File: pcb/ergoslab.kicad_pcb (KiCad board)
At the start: 2 copper layers, 114.5 x 101.4 mm, 102 parts, among them J1 L_B_LED, J2 R_B_LED, J3 SLAVE_LED, P1 OLED, P2 ICSP, SW0:0 SW_Push, SW0:1 SW_Push, SW0:2 SW_Push, SW0:3 SW_Push, SW0:4 SW_Push, SW1:0 SW_Push, SW1:1 SW_Push, SW1:2 SW_Push, SW1:3 SW_Push, SW1:4 SW_Push, SW2:0 SW_Push, SW2:1 SW_Push, SW2:2 SW_Push, SW2:3 SW_Push, SW2:4 SW_Push, SW3:0 SW_Push, SW3:1 SW_Push, SW3:2 SW_Push, SW3:3 SW_Push, SW3:4 SW_Push, SW3:5 SW_Push, SW4:1 SW_Push, SW4:2 SW_Push, SW4:3 SW_Push, SW4:4 SW_Push, SW4:5 SW_Push

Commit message: feat: update chicken
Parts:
- removed the REF** at (163.8, 88.2)
- added G***: LOGO, footprints:chicken, B.Cu at (177.5, 71.1)
- moved REF** 2.54 mm to (137.6, 46.5)
- moved REF** 1.78 mm to (163.6, 49.8)
- moved REF** 1.25 mm to (125.6, 120.5)
- moved REF** 1.14 mm to (106.2, 45.9)
- moved Drill 0.69 mm to (142.2, 123.5)
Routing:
- net Row3: track 153.2 -> 152.6 mm
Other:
- board size 114.5 x 101.4 mm -> 114.5 x 101.2 mm

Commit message: docs: add list of parts to order
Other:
- outline, holes or cut-outs redrawn
- board text added: "FIXME still need hole when we put LED here"

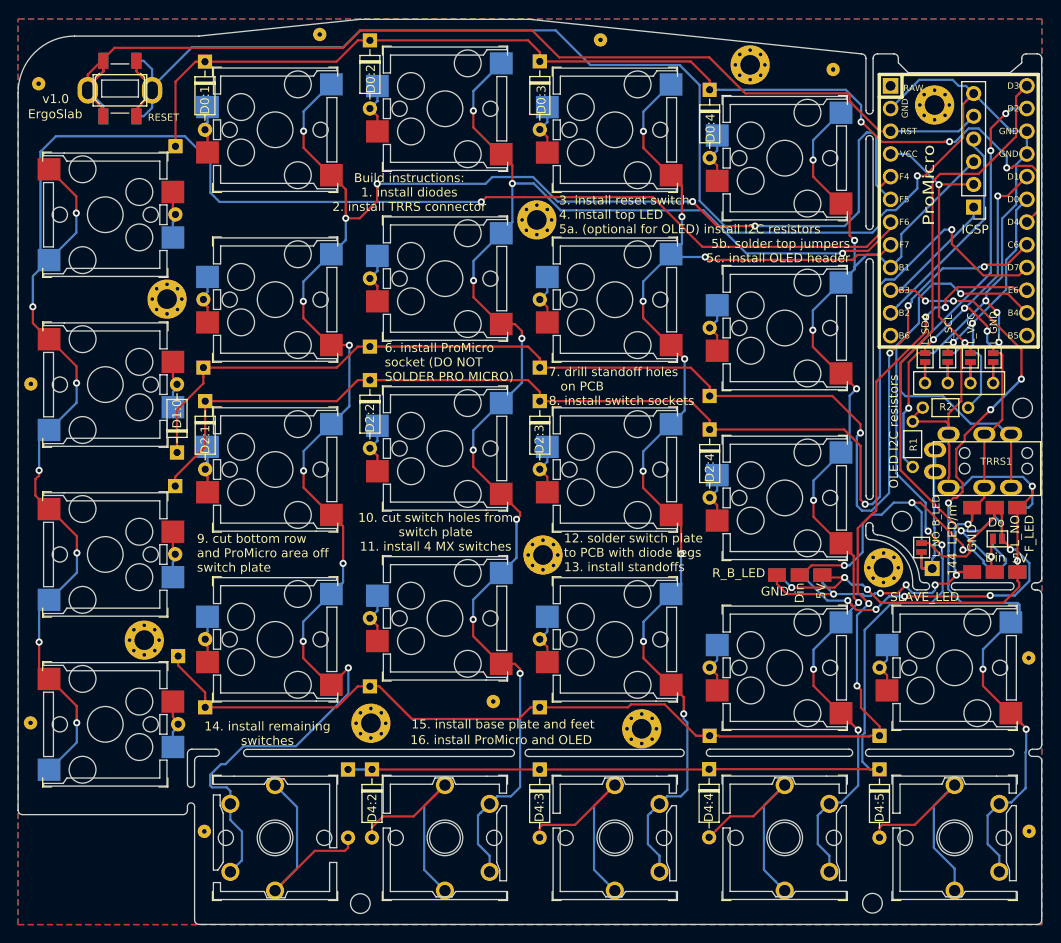
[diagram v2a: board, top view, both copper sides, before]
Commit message: fix: update single WS2812 footprint on PCB, had to expand space allocated for ProMicro
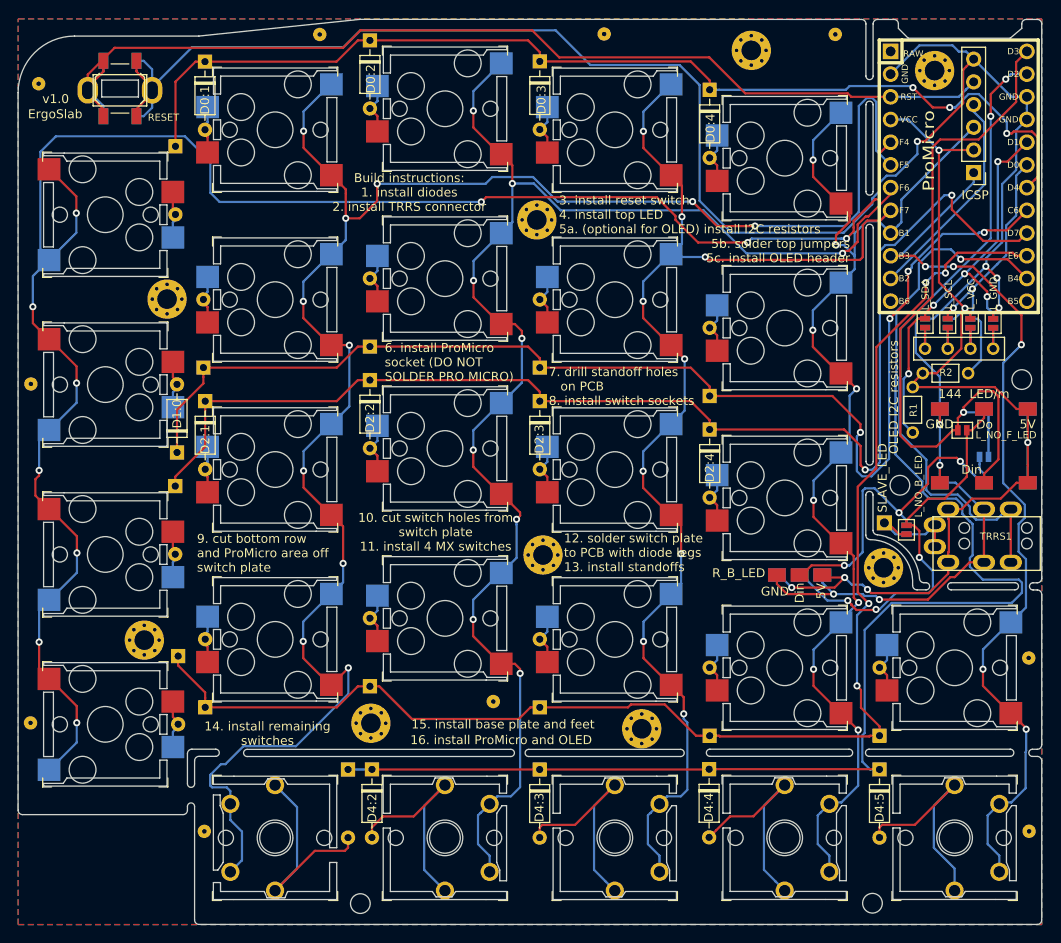
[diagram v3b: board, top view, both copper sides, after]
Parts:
- moved JP9 12.8 mm to (178.1, 90.2)
- moved LED_R1 10.7 mm to (180.5, 92.0)
- moved LED_L1 10.4 mm to (180.5, 91.8)
- moved JP12 9.28 mm to (180.5, 93.1)
- moved TRRS1 8.38 mm to (186.8, 102.8)
- moved J3 7.39 mm to (169.3, 100.5)
- moved HOLE_M2 4.03 mm to (171.1, 96.3)
- moved REF** 3.94 mm to (163.8, 45.9)
- moved JP1 3.85 mm to (181.5, 78.2)
- moved JP2 3.85 mm to (179.0, 78.2)
- moved JP6 3.85 mm to (179.0, 78.2)
- moved Drill 3.85 mm to (175.0, 49.9)
- moved P2 3.85 mm to (179.3, 61.4)
- moved PM1 3.85 mm to (177.7, 60.2)
- moved JP3 3.85 mm to (176.4, 78.2)
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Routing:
- net Row4: track 137.5 -> 158.5 mm, vias 3 -> 1
- net data: track 58.8 -> 72.4 mm
- net LED: track 77.7 -> 85.1 mm, vias 2 -> 1
- net SLAVE_LED: track 19.4 -> 12.1 mm
- net Net-(J1-Pad2): track 51.2 -> 44.4 mm, vias 5 -> 3
- net GND: track 255.2 -> 261.3 mm, vias 10 -> 8
- net Col4: track 124.6 -> 130.1 mm
- net Col5: track 107.4 -> 102.9 mm, vias 7 -> 5
- net Col1: track 203.0 -> 206.8 mm
- net Row2: track 144.3 -> 140.4 mm
- net Row1: track 142.1 -> 138.2 mm
- net Row3: track 152.6 -> 156.4 mm
- net Col3: track 131.2 -> 134.8 mm
- net Col2: track 159.9 -> 162.6 mm
- net Row0: track 122.4 -> 120.0 mm
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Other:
- outline, holes or cut-outs redrawn
- board text removed: "FIXME still need hole when we put LED here"
- board text removed: "L_NO F_LED"
- board text removed: "R_NO F_LED"

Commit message: fix: move dimensions off silk screen, change version 1.0=>0.1.0
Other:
- board text added: "v0.1.0"
- board text removed: "v1.0"
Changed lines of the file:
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@@
     (41 Cmts.User user)
     (42 Eco1.User user)
-    (43 Eco2.User user)
+    (43 Eco2.User user hide)
     (44 Edge.Cuts user)
     (45 Margin user)
     (46 B.CrtYd user)
     (47 F.CrtYd user)
-    (48 B.Fab user)
-    (49 F.Fab user)
+    (48 B.Fab user hide)
+    (49 F.Fab user hide)
   )
   (setup
@@
   (gr_arc (start 167.68 53.75) (end 168.08 53.75) (angle -180) (layer Edge.Cuts) (width 0.05))
   (gr_arc (start 167.68 50.54) (end 167.28 50.54) (angle -180) (layer Edge.Cuts) (width 0.05))
-  (gr_text v1.0 (at 76.65 53.1) (layer F.SilkS)
+  (gr_text v0.1.0 (at 76.3 53.2) (layer F.SilkS)
     (effects (font (size 1 1) (thickness 0.15)))
   )
@@
   (gr_line (start 183.41 46.31) (end 184.71 45.21) (layer Edge.Cuts) (width 0.05))
   (gr_line (start 172.01 46.31) (end 183.41 46.31) (layer Edge.Cuts) (width 0.05))
-  (dimension 101.37 (width 0.12) (layer F.SilkS)
-    (gr_text "101.370 mm" (at 68.377306 94.745 90) (layer F.SilkS)
+  (dimension 101.37 (width 0.12) (layer Dwgs.User)
+    (gr_text "101.370 mm" (at 68.377306 94.745 90) (layer Dwgs.User)
       (effects (font (size 1 1) (thickness 0.15)))
     )
@@
     (arrow2b (pts (xy 69.647306 145.43) (xy 69.060885 144.303496)))
   )
-  (dimension 114.56 (width 0.12) (layer F.SilkS)
-    (gr_text "114.560 mm" (at 129.63 41.44) (layer F.SilkS)
+  (dimension 114.56 (width 0.12) (layer Dwgs.User)
+    (gr_text "114.560 mm" (at 129.63 41.44) (layer Dwgs.User)
       (effects (font (size 1 1) (thickness 0.15)))
     )
